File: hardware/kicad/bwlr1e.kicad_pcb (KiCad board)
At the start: 2 copper layers, 36.8 x 90.9 mm, 65 parts, among them J1 Qwiic, Q1 AO3407, Q2 DMG1012UW, SW3 RESET, SW4 BOOT, U1 BME688, U2 RAK3172, U3 AEM10941-QFN, U4 XC6215

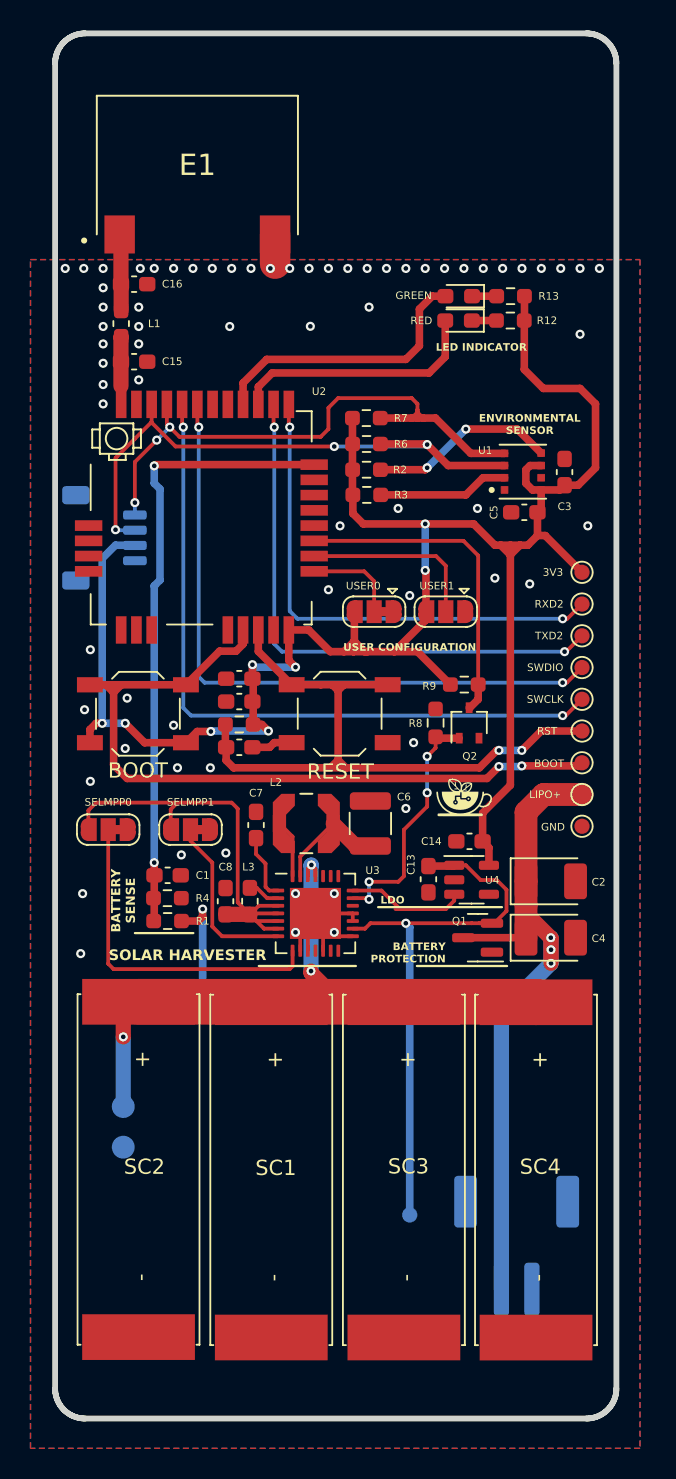
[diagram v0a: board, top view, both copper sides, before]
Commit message: improve silkscreen graphic and wiring
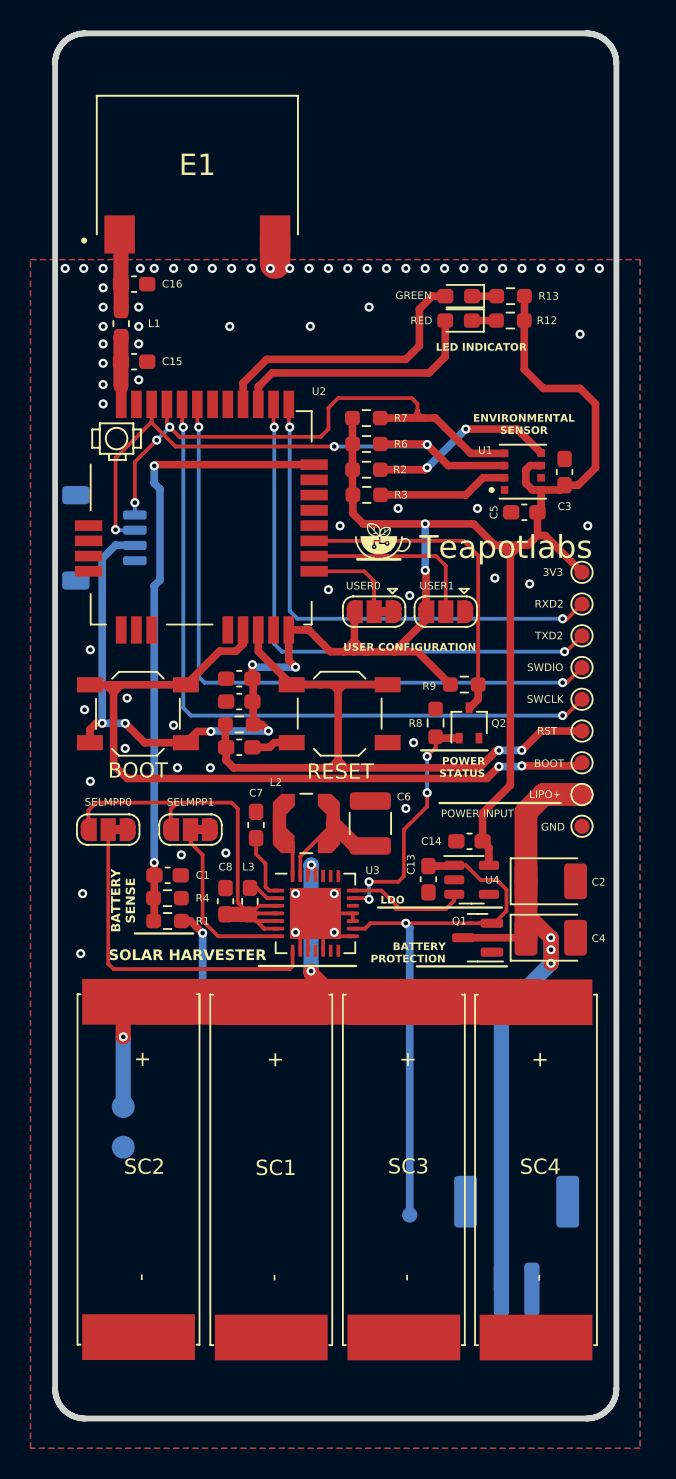
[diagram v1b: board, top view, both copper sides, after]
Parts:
- moved G*** 17.6 mm to (149.6, 86.5)
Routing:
- net /BATT+: track 60.3 -> 58.4 mm
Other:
- board text added: "POWER INPUT"
- board text added: "POWER STATUS"

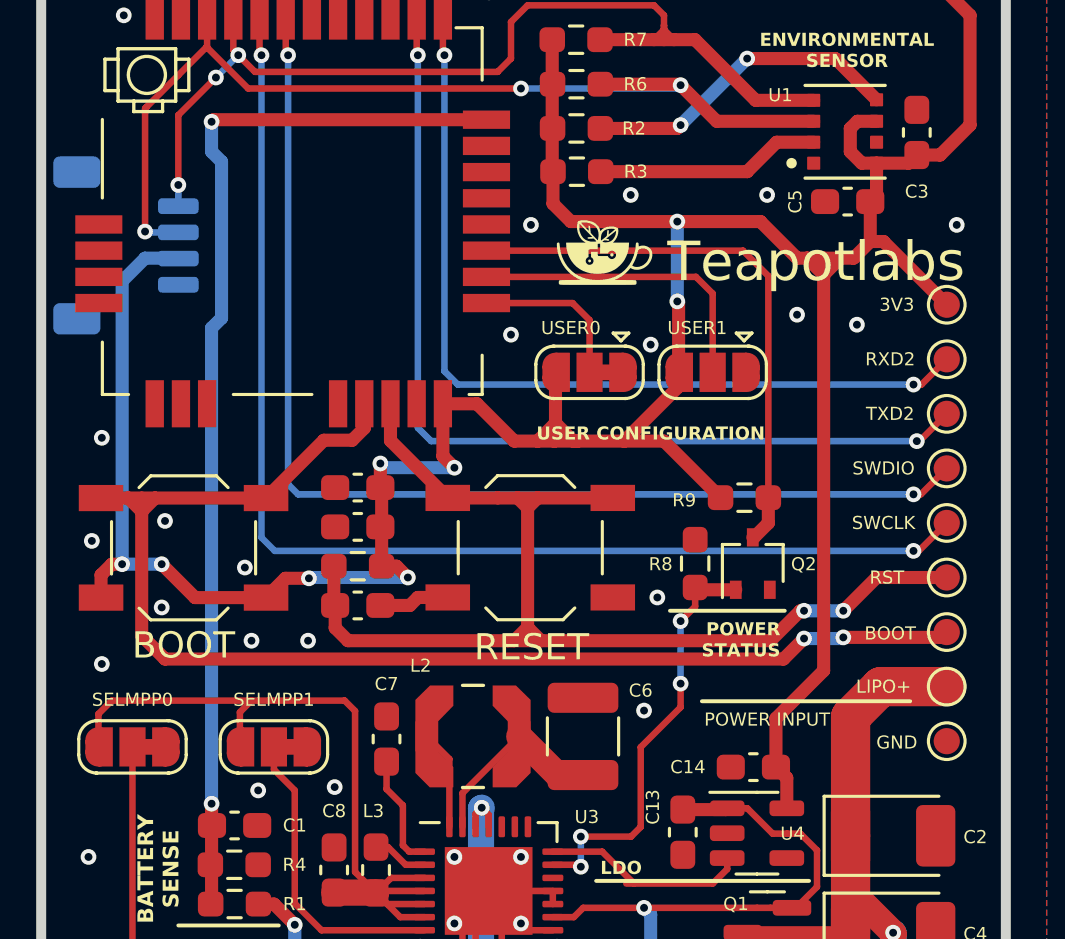
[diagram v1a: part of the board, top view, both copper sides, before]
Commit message: add gnd vias
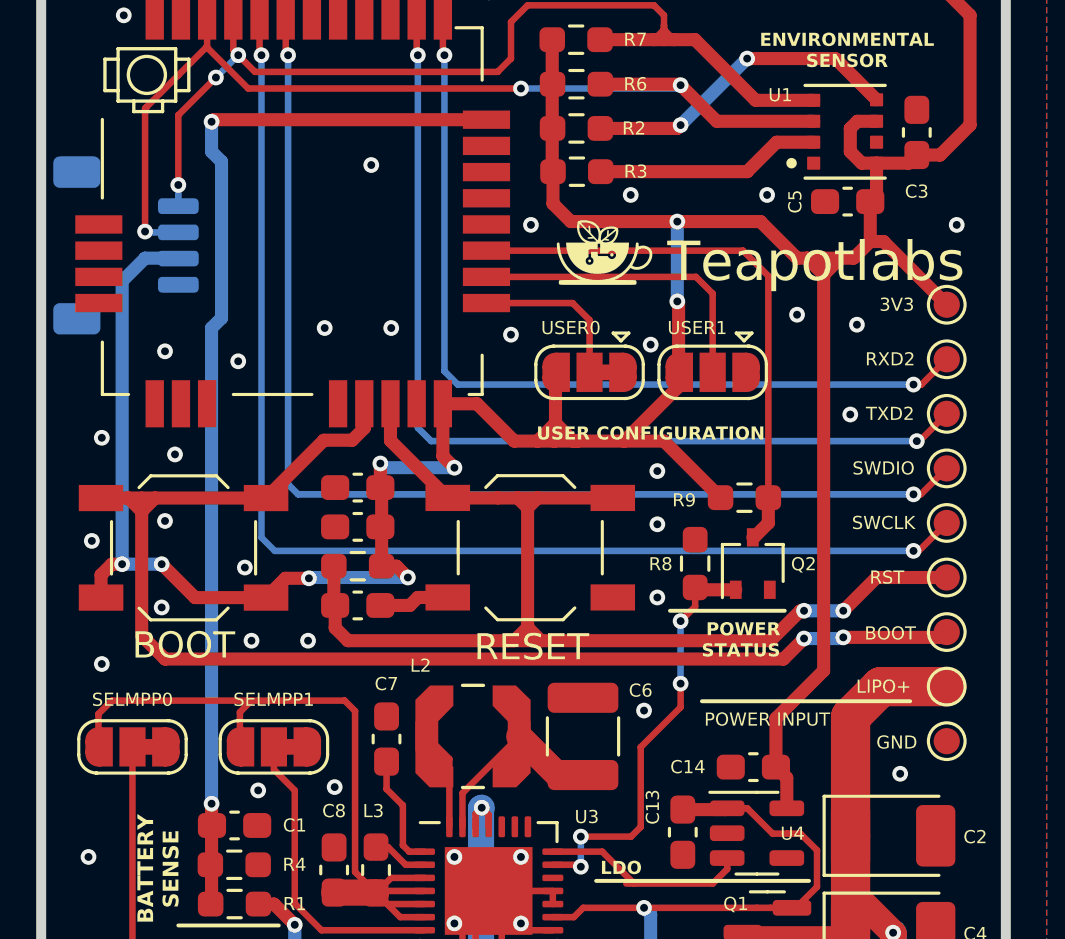
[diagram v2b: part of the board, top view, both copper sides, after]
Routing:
- net GND: vias 69 -> 79
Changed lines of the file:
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@@
   (segment (start 144.198 111.9) (end 145.198 110.9) (width 0.25) (layer "F.Cu") (net 2))
   (segment (start 142.55 66.35) (end 142.55 68.27) (width 2) (layer "F.Cu") (net 2))
+  (via (at 133.223 94.234) (size 0.6) (drill 0.3) (layers "F.Cu" "B.Cu") (free) (net 2))
   (via (at 139.573 72.39) (size 0.6) (drill 0.3) (layers "F.Cu" "B.Cu") (free) (net 2))
   (via (at 151.13 68.58) (size 0.6) (drill 0.3) (layers "F.Cu" "B.Cu") (free) (net 2))
   (via (at 135.89 98.552) (size 0.6) (drill 0.3) (layers "F.Cu" "B.Cu") (free) (net 2))
+  (via (at 159.004 92.71) (size 0.6) (drill 0.3) (layers "F.Cu" "B.Cu") (free) (net 2))
   (via (at 143.891 112.141) (size 0.6) (drill 0.3) (layers "F.Cu" "B.Cu") (net 2))
   (via (at 146.431 112.141) (size 0.6) (drill 0.3) (layers "F.Cu" "B.Cu") (net 2))
   (via (at 131.2672 73.533) (size 0.6) (drill 0.3) (layers "F.Cu" "B.Cu") (free) (net 2))
   (via (at 133.604 71.12) (size 0.6) (drill 0.3) (layers "F.Cu" "B.Cu") (free) (net 2))
+  (via (at 160.909 106.426) (size 0.6) (drill 0.3) (layers "F.Cu" "B.Cu") (free) (net 2))
   (via (at 160.02 68.58) (size 0.6) (drill 0.3) (layers "F.Cu" "B.Cu") (free) (net 2))
   (via (at 129.921 109.601) (size 0.6) (drill 0.3) (layers "F.Cu" "B.Cu") (free) (net 2))
@@
   (via (at 134.62 68.58) (size 0.6) (drill 0.3) (layers "F.Cu" "B.Cu") (free) (net 2))
   (via (at 133.7056 68.58) (size 0.6) (drill 0.3) (layers "F.Cu" "B.Cu") (free) (net 2))
+  (via (at 132.842 90.297) (size 0.6) (drill 0.3) (layers "F.Cu" "B.Cu") (free) (net 2))
   (via (at 133.604 73.533) (size 0.6) (drill 0.3) (layers "F.Cu" "B.Cu") (free) (net 2))
   (via (at 133.604 75.8952) (size 0.6) (drill 0.3) (layers "F.Cu" "B.Cu") (free) (net 2))
+  (via (at 140.716 83.185) (size 0.6) (drill 0.3) (layers "F.Cu" "B.Cu") (free) (net 2))
   (via (at 153.67 68.58) (size 0.6) (drill 0.3) (layers "F.Cu" "B.Cu") (free) (net 2))
   (via (at 138.303 101.346) (size 0.6) (drill 0.3) (layers "F.Cu" "B.Cu") (free) (net 2))
   (via (at 161.29 68.58) (size 0.6) (drill 0.3) (layers "F.Cu" "B.Cu") (free) (net 2))
   (via (at 128.778 68.58) (size 0.6) (drill 0.3) (layers "F.Cu" "B.Cu") (free) (net 2))
+  (via (at 138.938 89.408) (size 0.6) (drill 0.3) (layers "F.Cu" "B.Cu") (free) (net 2))
   (via (at 131.2672 74.803) (size 0.6) (drill 0.3) (layers "F.Cu" "B.Cu") (free) (net 2))
   (via (at 154.94 68.58) (size 0.6) (drill 0.3) (layers "F.Cu" "B.Cu") (free) (net 2))
@@
   (via (at 151.384 90.043) (size 0.6) (drill 0.3) (layers "F.Cu" "B.Cu") (free) (net 2))
   (via (at 163.83 68.58) (size 0.6) (drill 0.3) (layers "F.Cu" "B.Cu") (free) (net 2))
+  (via (at 151.638 96.901) (size 0.6) (drill 0.3) (layers "F.Cu" "B.Cu") (free) (net 2))
   (via (at 142.24 68.58) (size 0.6) (drill 0.3) (layers "F.Cu" "B.Cu") (free) (net 2))
   (via (at 148.59 68.58) (size 0.6) (drill 0.3) (layers "F.Cu" "B.Cu") (free) (net 2))
+  (via (at 135.636 90.678) (size 0.6) (drill 0.3) (layers "F.Cu" "B.Cu") (free) (net 2))
   (via (at 162.56 72.898) (size 0.6) (drill 0.3) (layers "F.Cu" "B.Cu") (free) (net 2))
   (via (at 131.2672 77.47) (size 0.6) (drill 0.3) (layers "F.Cu" "B.Cu") (free) (net 2))
   (via (at 138.43 68.58) (size 0.6) (drill 0.3) (layers "F.Cu" "B.Cu") (free) (net 2))
+  (via (at 141.478 89.408) (size 0.6) (drill 0.3) (layers "F.Cu" "B.Cu") (free) (net 2))
   (via (at 136.144 101.346) (size 0.6) (drill 0.3) (layers "F.Cu" "B.Cu") (free) (net 2))
   (via (at 130.429 102.235) (size 0.6) (drill 0.3) (layers "F.Cu" "B.Cu") (free) (net 2))
@@
   (via (at 130.429 93.599) (size 0.6) (drill 0.3) (layers "F.Cu" "B.Cu") (free) (net 2))
   (via (at 130.048 97.536) (size 0.6) (drill 0.3) (layers "F.Cu" "B.Cu") (free) (net 2))
+  (via (at 151.638 94.869) (size 0.6) (drill 0.3) (layers "F.Cu" "B.Cu") (free) (net 2))
   (via (at 133.604 72.39) (size 0.6) (drill 0.3) (layers "F.Cu" "B.Cu") (free) (net 2))
   (via (at 146.05 89.662) (size 0.6) (drill 0.3) (layers "F.Cu" "B.Cu") (free) (net 2))

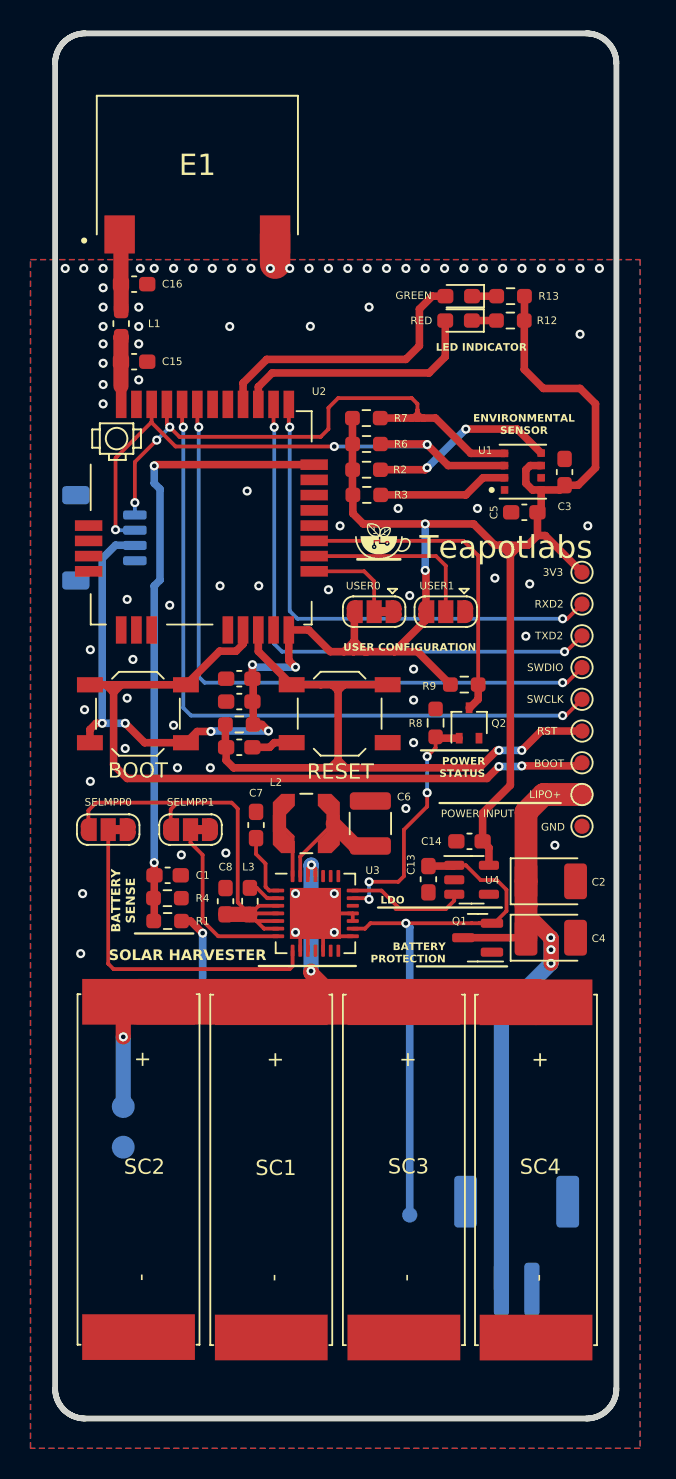
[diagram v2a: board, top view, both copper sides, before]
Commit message: fix led polarity and minor wiring changes
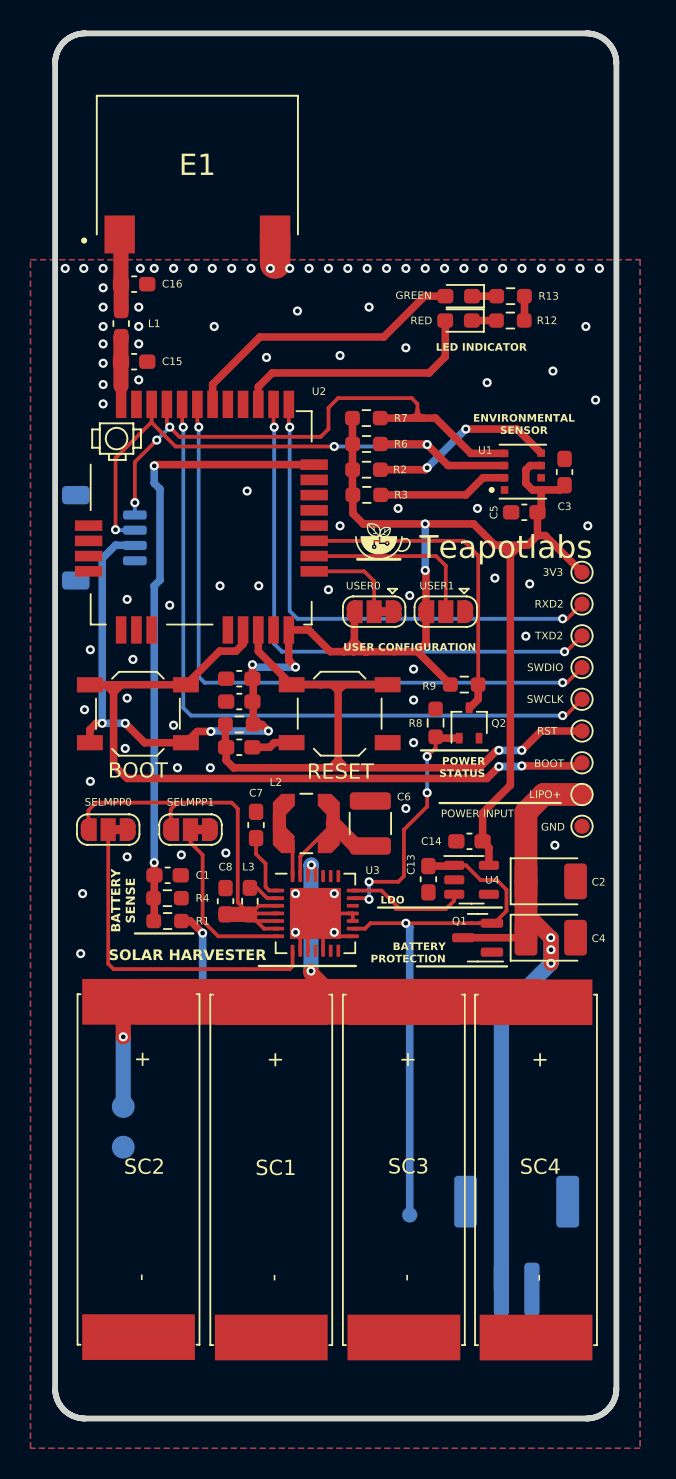
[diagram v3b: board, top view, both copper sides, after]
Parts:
- C2, C4: value 330uF -> 330u
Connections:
- R12 pad 1: +3V3 -> GND
- R13 pad 1: +3V3 -> GND
- U2 pad 4: /LED2 -> unconnected-(U2-UART1_TX/PB6-Pad4)
- U2 pad 6: unconnected-(U2-PA1-Pad6) -> /LED2
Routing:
- net +3V3: track 135.9 -> 118.1 mm
- net GND: track 19.1 -> 20.7 mm, vias 79 -> 86
- net /LED2: track 18.4 -> 19.0 mm

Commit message: change library to project-level and minor changes
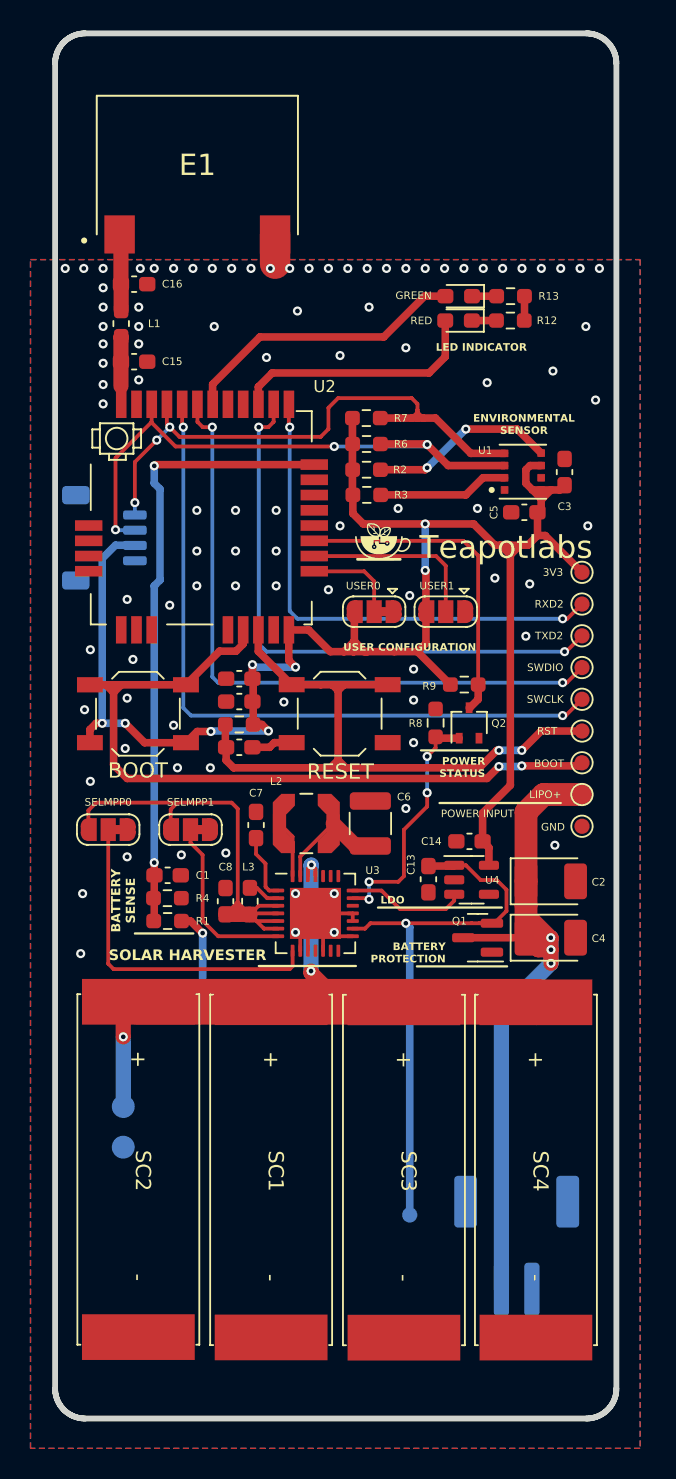
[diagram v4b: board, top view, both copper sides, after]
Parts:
- BT1: footprint Connector_JST:JST_PH_S2B-PH-SM4-TB_1x02-1MP_P2.00mm_Horizontal -> bwlr1e:JST_PH_S2B-PH-SM4-TB_1x02-1MP_P2.00mm_Horizontal
- E1: footprint Teapot:XDCR_ANT-915-USP410 -> bwlr1e:XDCR_ANT-915-USP410
- G***: footprint Teapot:TeapotLogo4mm -> bwlr1e:TeapotLogo4mm
- G***: footprint Teapot:TeapotLogo -> bwlr1e:TeapotLogo
- J1: footprint Connector_JST:JST_SH_SM04B-SRSS-TB_1x04-1MP_P1.00mm_Horizontal -> bwlr1e:JST_SH_SM04B-SRSS-TB_1x04-1MP_P1.00mm_Horizontal
- L2: footprint Teapot:IND_LPS4012-103MRB -> bwlr1e:IND_LPS4012-103MRB
- REF**: value EdgeCut_BWLR1D -> EdgeCut_BWLR1E; footprint Teapot:EdgeCut_BWLR1D -> bwlr1e:EdgeCut_BWLR1E
- SC1, SC2, SC3, SC4: footprint Teapot:KXOB25-05X3F -> bwlr1e:KXOB25-05X3F
- U1: footprint Teapot:BME680-PSON80P300X300X100-8N -> bwlr1e:BME680-PSON80P300X300X100-8N
- U2: footprint Teapot:RAK3172 -> bwlr1e:RAK3172
- moved U2 10.8 mm to (137.7, 84.9)
- moved SC2 0.31 mm to (133.6, 127.7)
- moved SC1 0.31 mm to (142.3, 127.7)
- moved SC4 0.31 mm to (159.7, 127.7)
- moved SC3 0.30 mm to (151.0, 127.7)
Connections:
- U4 pad 4: (no net) -> unconnected-(U4-NC-Pad4)
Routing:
- net /LIPO+: track 45.4 -> 49.0 mm
- net /BUCK: track 30.5 -> 32.4 mm
- net /TXD2: track 36.6 -> 38.3 mm
- net +3V3: track 118.1 -> 119.8 mm
- net GND: vias 86 -> 93

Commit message: small improvement and add production info
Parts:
- C15, C16: value ? F -> DNP
- C2, C4: value 330u -> 47u
- L1: value ? H -> 0
- L2: value 10uH 0.55A -> 10u
- Q1: value AO3407 -> AO3407A
- U2: value RAK3172 -> RAK3172-T
- U3: value AEM10941-QFN -> AEM10941
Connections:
- D1 pad 2: /LED1 -> /LED0
- D2 pad 2: /LED2 -> /LED1
- U2 pad 3: /LED1 -> /LED0
- U2 pad 6: /LED2 -> /LED1
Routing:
- net /LED2: track 19.0 -> 0.00 mm
- net /LED0: track 0.00 -> 16.6 mm
- net /LED1: track 16.6 -> 19.0 mm
